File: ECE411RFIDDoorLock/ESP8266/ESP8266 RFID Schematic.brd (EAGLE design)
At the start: 160 x 100 mm, 21 parts, among them T1 2N2222, T2 2N2222, X1 ESP-12E

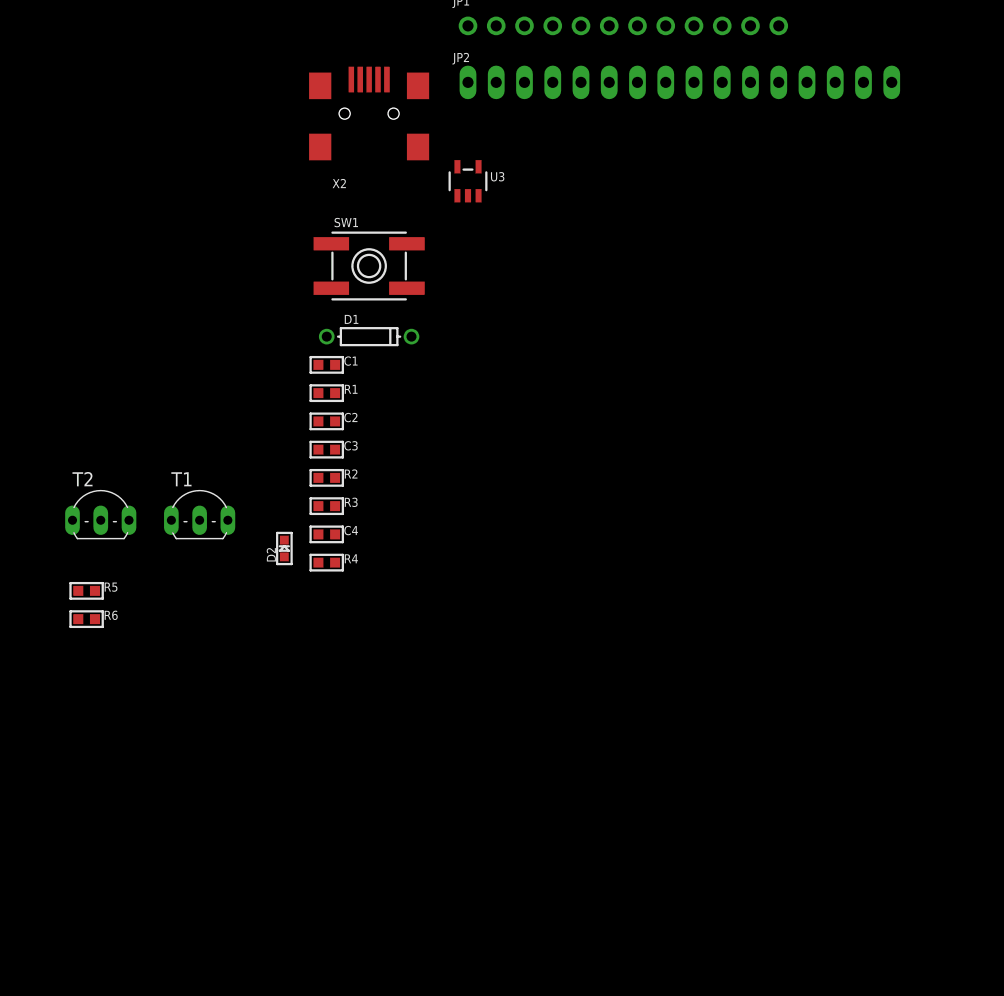
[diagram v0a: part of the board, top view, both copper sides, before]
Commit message: Update ESP8266 RFID Schematic.brd
Added servo, RFID sensor, LIPO power port, and better labeling to schematic, did not work on board layout
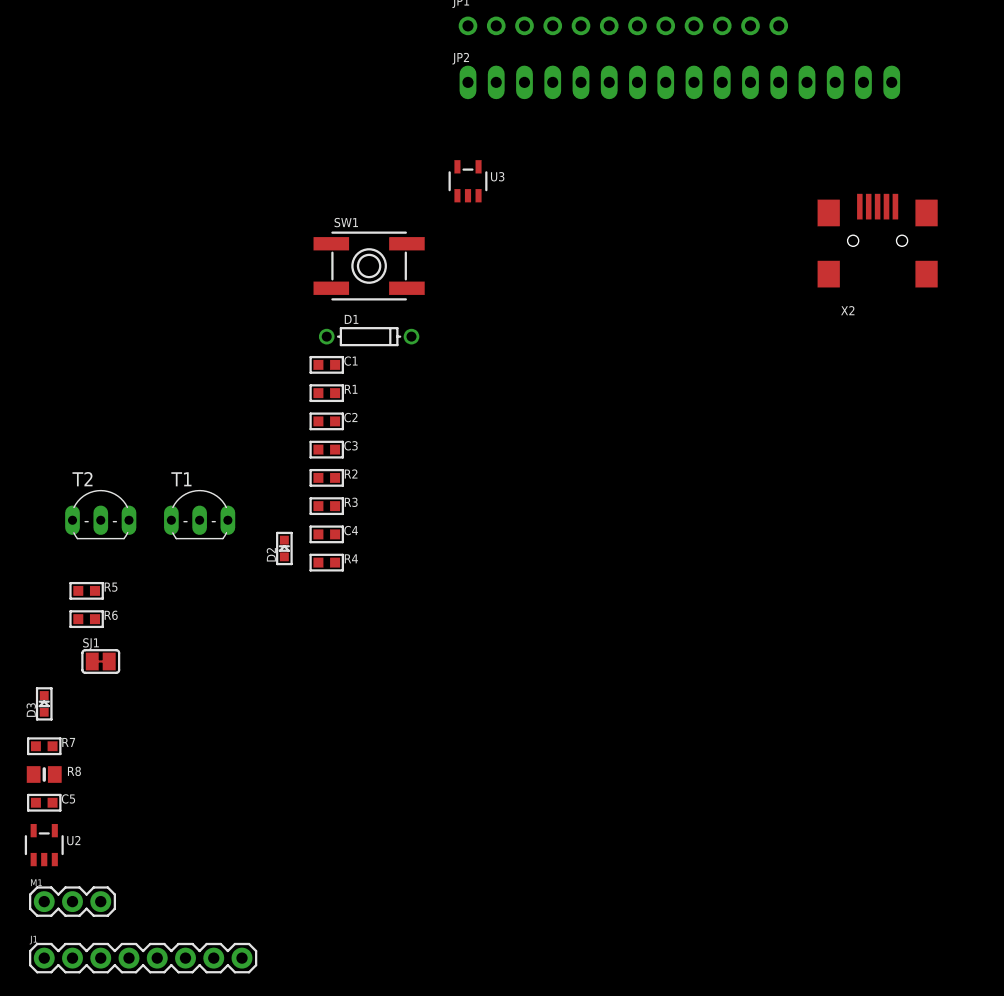
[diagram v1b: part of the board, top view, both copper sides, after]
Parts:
- added C5, R7: (no value), microbuilder:0603-MINI
- added D3: (no value), microbuilder:CHIPLED_0603
- added J1: (no value), SparkFun-Connectors:1X08
- added M1: SERVO, SparkFun-Electromechanical:1X03
- added R8: (no value), microbuilder:0805-NO
- added SJ1: (no value), microbuilder:SOLDERJUMPER_CLOSEDWIRE
- added U2: (no value), microbuilder:SOT23-5
- moved X2 47.1 mm to (15.2, -24.1)
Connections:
- new net N$10: SJ1.2, U2.3
- new net N$11: R8.1, U2.5
- new net N$8: D3.C, R7.1
- new net N$9: R7.2, U2.1
- net 3.3V: now also J1.8
- net GND: now also C5.2, J1.6, R8.2, U2.2
- net GPIO12/MISO: now also J1.4
- net GPIO13/MOSI: now also J1.3
- net GPIO14/SCK: now also J1.2
- net GPIO15: now also J1.1
- net GPIO4/SDA: now also M1.1
- net VBAT: now also C5.1, M1.2, M1.3, SJ1.1
- net VBUS: now also D3.A, U2.4

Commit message: First pass at PCB layout
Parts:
- removed C5: (no value), microbuilder:0603-MINI
- removed D1: (no value), microbuilder:DO-1N4148
- removed D3: (no value), microbuilder:CHIPLED_0603
- removed JP1: (no value), microbuilder:1X12_ROUND
- removed JP2: (no value), microbuilder:1X16_OVAL
- removed R8: (no value), microbuilder:0805-NO
- removed SJ1: (no value), microbuilder:SOLDERJUMPER_CLOSEDWIRE
- removed U2: (no value), microbuilder:SOT23-5
- removed X2: (no value), microbuilder:USB-MINIB
- added D4: MBR0540, microbuilder:SOD-123
- added J2, J3: (no value), SparkFun-Connectors:1X02
- added JP4: (no value), microbuilder:1X16_ROUND
- added JP5: (no value), microbuilder:1X12_ROUND
- added Q3: DMG341, microbuilder:SOT23-R
- added X4: 20329, microbuilder:4UCONN_20329_V2
- C2, C3: value (none) -> 10µF
- R1, R7: value (none) -> 10k
- T1, T2: value 2N2222 -> 600mA/40V; device adafruit:TO92-EBC-OVAL -> SparkFun-DiscreteSemi:SOT23-3
- U3: value (none) -> AP2112-3.3
- moved J1 128.0 mm to (30.5, 3.17)
- moved R7 118.2 mm to (15.2, 22.9), turned to 270 degrees
- moved M1 117.3 mm to (20.3, 3.17)
- moved R6 114.6 mm to (17.1, 31.1), turned to 180 degrees
- moved R5 111.8 mm to (21.0, 26.7), turned to 90 degrees
- moved T2 109.1 mm to (22.2, 30.5), turned to 270 degrees
- moved T1 97.3 mm to (17.1, 27.3), turned to 180 degrees
- moved R3 93.6 mm to (23.5, 26.7), turned to 270 degrees
- moved R4 92.6 mm to (21.0, 22.2), turned to 270 degrees
- moved R2 92.2 mm to (11.4, 35.6), turned to 180 degrees
- moved D2 90.5 mm to (21.0, 17.8)
- moved C4 85.5 mm to (4.45, 26.7), turned to 270 degrees
- moved SW1 81.0 mm to (19.9, 38.0), turned to 90 degrees
- moved C3 78.6 mm to (10.2, 22.9), turned to 90 degrees
- moved C2 75.0 mm to (7.62, 22.9), turned to 90 degrees
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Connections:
- removed net N$1: JP1.2, R1.1, U3.3
- removed net N$11: R8.1, U2.5
- removed net OUT: C2.1, C3.1, U3.5
- new net EN: JP5.2
- new net N$14: C4.1, U1.5, U1.6
- net 3.3V: now also C2.1, C3.1, JP4.15, U3.5; no longer C4.1, JP2.15, U1.5, U1.6
- net ADC: now also JP4.12; no longer JP2.12
- net CH_PD: now also JP4.1; no longer JP2.1
- net DTR: now also T1.2; no longer T1.E
- net GND: now also J2.1, J3.1, JP4.13, M1.3, R7.1, X4.BASE@1, X4.BASE@2, X4.GND, X4.SPRT@1, X4.SPRT@2, X4.SPRT@3, X4.SPRT@4; no longer C5.2, JP2.13, R8.2, U2.2, X2.GND, X2.GND1, X2.GND2, X2.GND3, X2.GND4
- net GPIO0: now also JP5.8, T1.3; no longer JP1.8, T1.C
- net GPIO12/MISO: now also JP4.4, JP5.5; no longer JP1.5, JP2.4
- net GPIO13/MOSI: now also JP4.5, JP5.6; no longer JP1.6, JP2.5
- net GPIO14/SCK: now also JP4.6, JP5.4; no longer JP1.4, JP2.6
- net GPIO15: now also JP5.7; no longer JP1.7
- net GPIO16: now also JP5.9; no longer JP1.9
- net GPIO2: now also JP5.10; no longer JP1.10
- net GPIO4/SDA: now also JP5.12; no longer JP1.12
- net GPIO5/SCL: now also J3.2, JP5.11; no longer JP1.11
- net N$10: now also R1.1, U3.3; no longer SJ1.2, U2.3
- net N$2: now also X4.VBUS; no longer X2.VBUS
- net N$3: now also X4.D+; no longer X2.D+
- net N$4: now also X4.D-; no longer X2.D-
- net N$6: now also T1.1; no longer T1.B
- net N$7: now also T2.1; no longer T2.B
- net N$8: now also C1.1, D4.C, Q3.2, R1.2, U3.1; no longer D3.C, R7.1
- net N$9: now also D4.A, Q3.1; no longer U2.1
- net RESET: now also JP4.16, T2.3; no longer JP2.16, T2.C
- net RTS: now also T2.2; no longer T2.E
- net RXD: now also JP4.3; no longer JP2.3
- net TXD: now also JP4.2; no longer JP2.2
- net VBAT: now also J2.2, JP5.1, Q3.3; no longer C5.1, D1.A, JP1.1, M1.3, SJ1.1
- net VBUS: now also JP5.3; no longer C1.1, D1.C, D3.A, JP1.3, U2.4, U3.1
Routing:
- net RESET: track 0.00 -> 62.7 mm, vias 0 -> 1
- net TXD: track 0.00 -> 42.8 mm, vias 0 -> 4
- net GPIO12/MISO: track 0.00 -> 38.4 mm, vias 0 -> 2
- net RXD: track 0.00 -> 35.7 mm, vias 0 -> 2
- net VBAT: track 0.00 -> 31.8 mm, vias 0 -> 1
- net GPIO13/MOSI: track 0.00 -> 31.4 mm
- net GPIO15: track 0.00 -> 31.1 mm, vias 0 -> 3
- net GPIO14/SCK: track 0.00 -> 30.6 mm, vias 0 -> 1
- net N$8: track 0.00 -> 29.9 mm, vias 0 -> 2
- net GND: track 0.00 -> 24.4 mm, vias 0 -> 10
- net N$4: track 0.00 -> 17.6 mm, vias 0 -> 2
- net RTS: track 0.00 -> 16.7 mm, vias 0 -> 2
- net DTR: track 0.00 -> 15.4 mm
- net N$2: track 0.00 -> 14.7 mm, vias 0 -> 2
- net N$3: track 0.00 -> 13.9 mm
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- added copper zone on layer 1, net 3.3V
- added copper zone on layer 16, net GND
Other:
- board size 160 x 100 mm -> 61 x 43.8 mm

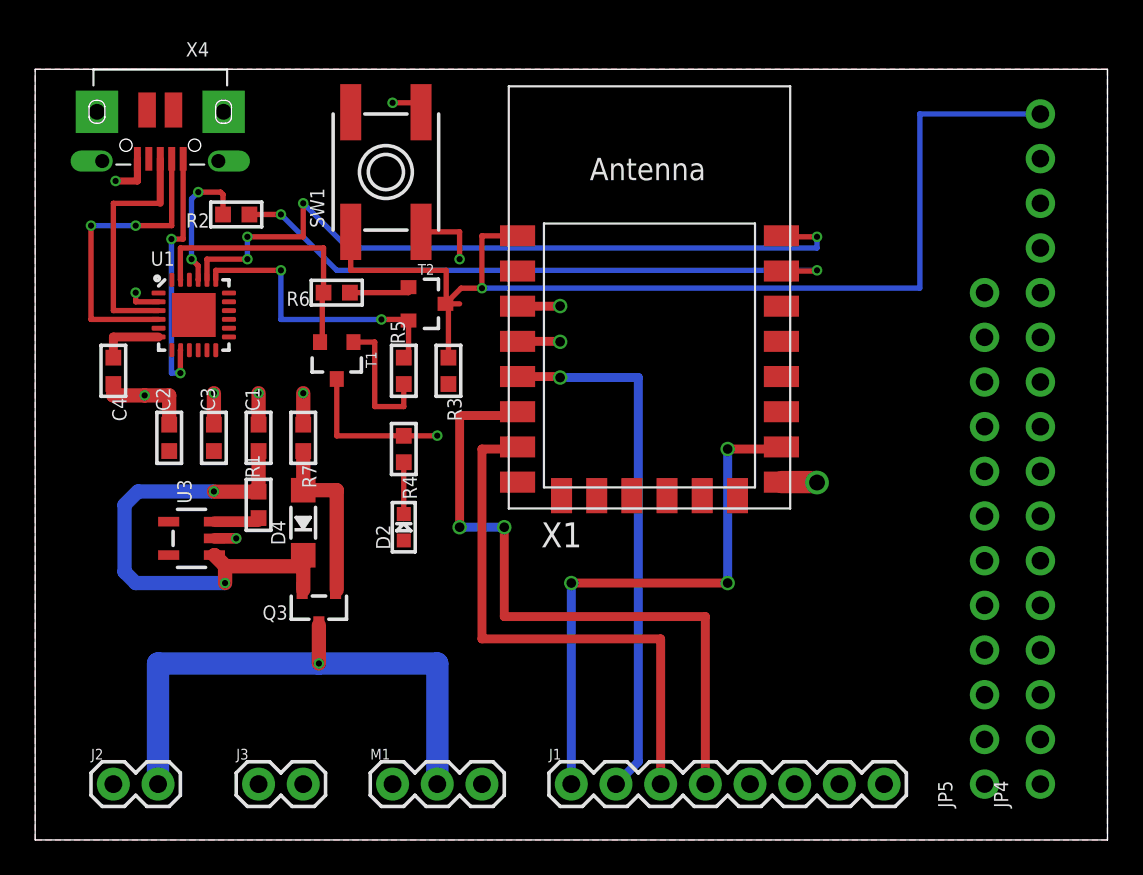
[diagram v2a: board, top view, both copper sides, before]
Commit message: Traces Routed
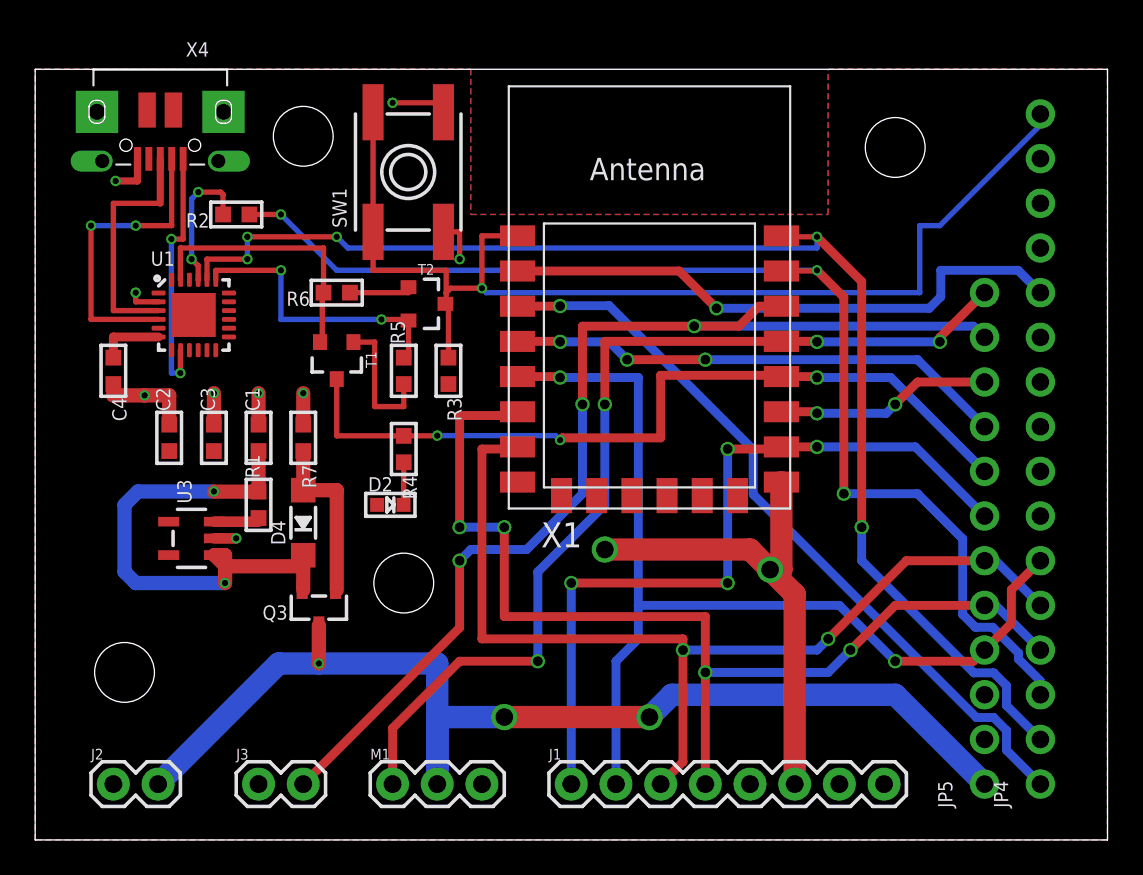
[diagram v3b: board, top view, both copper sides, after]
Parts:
- moved D2 1.48 mm to (20.2, 19.1), turned to 270 degrees
- moved SW1 1.27 mm to (21.2, 38.0)
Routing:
- net GPIO5/SCL: track 0.00 -> 63.0 mm, vias 0 -> 3
- net GPIO4/SDA: track 0.00 -> 55.7 mm, vias 0 -> 4
- net CH_PD: track 2.43 -> 43.2 mm
- net GPIO0: track 8.95 -> 46.0 mm, vias 1 -> 3
- net VBAT: track 31.8 -> 65.3 mm, vias 1 -> 3
- net ADC: track 0.00 -> 32.9 mm, vias 0 -> 1
- net RXD: track 35.7 -> 68.1 mm, vias 2 -> 3
- net TXD: track 42.8 -> 74.6 mm, vias 4 -> 5
- net GPIO14/SCK: track 30.6 -> 58.2 mm, vias 1 -> 2
- net GND: track 24.4 -> 50.6 mm, vias 10 -> 11
- net GPIO16: track 2.44 -> 28.6 mm, vias 1 -> 3
- net GPIO13/MOSI: track 31.4 -> 56.6 mm, vias 0 -> 2
- net GPIO12/MISO: track 38.4 -> 60.1 mm, vias 2 -> 4
- net GPIO15: track 31.1 -> 44.3 mm, vias 3 -> 4
- net GPIO2: track 0.00 -> 12.3 mm, vias 0 -> 2
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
